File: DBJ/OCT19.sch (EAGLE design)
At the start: 30 parts, among them IC1 ATMEGA168TQFP-08, IC2 TB6612FNG, IC3 7805DT, J1 5.5x2.1mm Barrel, Y2 16MHZ

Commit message: Hbridge
entire hbridge circuit, changed any remaining thru-hole to smd, used a
different hbridge, organized the schematic,
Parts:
- removed IC2: TB6612FNG, adafruit:TB6612FNG
- removed LED1, LED2, LED3, PWR_LED, SCK_LED: (no value), eagle-ltspice:LED_E
- removed R7, R8: (no value), SparkFun-Resistors:RESISTORPTH-1/4W
- added C5: (no value), adafruit:C-US025-024X044
- added IC4: L298, st-microelectronics:L298
- added LD1, LD2: PL006-WCR12, led:PL006-WCR12
- added OK1, OK2: PC827, optocoupler:PC827
- added R2(SMD), R5, R6: (no value), adafruit:R-US_M0805
- added X1-MOT1, X2-MOT2: (no value), con-wago-500:W237-102
- C3: value 0.1uF -> (none); device SparkFun-Capacitors:0.1UF-25V(+80/-20%)(0603) -> adafruit:C-US025-024X044
- R1, R2, R3, R4: device SparkFun-Resistors:RESISTORPTH-1/4W -> adafruit:R-US_M0805
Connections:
- removed net N$12: PWR_LED.C, R8.1
- new net N$13: IC4.SEN_A, R5.1
- new net N$14: IC4.SEN_B, R6.1
- new net N$15: IC4.OUT2, X2-MOT2-1.KL
- new net N$2: LD2.A, R2.2
- new net N$3: OK1A.A, R3.1
- new net N$4: IC4.ENABLE_A, OK1A.COL
- new net N$5: OK2A.A, R4.1
- new net N$6: IC4.ENABLE_B, OK2A.COL
- new net N$7: IC4.OUT1, X2-MOT2-2.KL
- new net N$8: IC4.OUT3, X1-MOT1-2.KL
- new net N$9: IC4.OUT4, X1-MOT1-1.KL
- net +12V: now also C5.1, IC4.VS
- net +5V: now also C3.1, IC4.INPUT1, IC4.INPUT2, IC4.INPUT3, IC4.INPUT4, IC4.VCC, R2(SMD).2, R2.1; no longer PWR_LED.A, R1.2
- net GND: now also C3.2, C4.1, C5.2, IC4.GND, LD1.C, LD2.C, OK1A.C, OK1A.EMIT, OK2A.C, OK2A.EMIT, R5.2, R6.2; no longer R8.2, SCK_LED.C
- net N$1: now also R2(SMD).1; no longer R1.1
- net N$10: now also LD1.A, R1.1; no longer R7.2, SCK_LED.A
- net PD4: now also R4.2
- net PD5: now also R3.2
- net SCK: now also R1.2; no longer R7.1
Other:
- note added: "Barrel-Jack and Voltage Regulation"
- note added: "HBridge/Motor Controls"
- note added: "LCD"
- note added: "LED Indicators"
- moved on the sheet: C1, C2, C3, C4, IC1, IC3, ISP1, J1, R1, R2, R3, R4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

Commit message: Add files via upload
Redid the crystal wiring, and edited the RST of the ICSP
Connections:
- removed net XTAL1: IC1.PB6(XTAL1/TOSC1), Y2.3
- removed net XTAL2: IC1.PB7(XTAL2/TOSC2), Y2.1
- new net N$11: IC1.PB6(XTAL1/TOSC1), Y2.1
- new net N$16: IC1.PB7(XTAL2/TOSC2), Y2.3
- new net N$17: C4.1, ISP1.RST
- net GND: no longer C4.1
- net N$1: no longer ISP1.RST
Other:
- moved on the sheet: Y2
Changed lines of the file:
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@@
 <?xml version="1.0" encoding="utf-8"?>
 <!DOCTYPE eagle SYSTEM "eagle.dtd">
-<eagle version="7.7.0">
+<eagle version="7.6.0">
 <drawing>
 <settings>
@@
 <part name="CN4" library="adafruit" deviceset="JST_3PIN" device=""/>
 <part name="OK1" library="optocoupler" deviceset="PC827" device=""/>
-<part name="GND14" library="supply1" deviceset="GND" device=""/>
 <part name="R2(SMD)" library="adafruit" deviceset="R-US_" device="M0805"/>
 <part name="R1" library="adafruit" deviceset="R-US_" device="M0805"/>
@@
 <instance part="P+2" gate="1" x="96.52" y="195.58"/>
 <instance part="GND1" gate="1" x="83.82" y="177.8"/>
-<instance part="Y2" gate="G$1" x="162.56" y="129.54" rot="R270"/>
-<instance part="GND2" gate="1" x="152.4" y="124.46"/>
+<instance part="Y2" gate="G$1" x="182.88" y="129.54" rot="R270"/>
+<instance part="GND2" gate="1" x="167.64" y="124.46"/>
 <instance part="GND3" gate="1" x="187.96" y="96.52"/>
 <instance part="C1" gate="G$1" x="101.6" y="185.42"/>
@@
 <instance part="CN4" gate="G$1" x="345.44" y="101.6" rot="MR0"/>
 <instance part="OK1" gate="A" x="76.2" y="259.08" rot="R270"/>
-<instance part="GND14" gate="1" x="170.18" y="157.48" rot="R270"/>
 <instance part="R2(SMD)" gate="G$1" x="187.96" y="165.1" rot="R90"/>
 <instance part="R1" gate="G$1" x="320.04" y="187.96" rot="R90"/>
@@
 </segment>
 </net>
-<net name="XTAL1" class="0">
-<segment>
-<pinref part="IC1" gate="G$1" pin="PB6(XTAL1/TOSC1)"/>
-<wire x1="190.5" y1="132.08" x2="182.88" y2="132.08" width="0.1524" layer="91"/>
-<label x="182.88" y="132.08" size="1.778" layer="95"/>
-</segment>
-<segment>
-<pinref part="Y2" gate="G$1" pin="3"/>
-<wire x1="162.56" y1="127" x2="167.64" y2="127" width="0.1524" layer="91"/>
-<label x="167.64" y="127" size="1.778" layer="95"/>
-</segment>
-</net>
-<net name="XTAL2" class="0">
-<segment>
-<pinref part="IC1" gate="G$1" pin="PB7(XTAL2/TOSC2)"/>
-<wire x1="190.5" y1="127" x2="185.42" y2="127" width="0.1524" layer="91"/>
-<label x="185.42" y="127" size="1.778" layer="95"/>
-</segment>
-<segment>
-<pinref part="Y2" gate="G$1" pin="1"/>
-<wire x1="162.56" y1="132.08" x2="167.64" y2="132.08" width="0.1524" layer="91"/>
-<label x="165.1" y="132.08" size="1.778" layer="95"/>
-</segment>
-</net>
 <net name="GND" class="0">
-<segment>
-<pinref part="Y2" gate="G$1" pin="2"/>
-<pinref part="GND2" gate="1" pin="GND"/>
-<wire x1="154.94" y1="129.54" x2="152.4" y2="129.54" width="0.1524" layer="91"/>
-<wire x1="152.4" y1="129.54" x2="152.4" y2="127" width="0.1524" layer="91"/>
-</segment>
 <segment>
 <pinref part="GND3" gate="1" pin="GND"/>
@@
 </segment>
 <segment>
-<pinref part="C4" gate="G$1" pin="1"/>
-<pinref part="GND14" gate="1" pin="GND"/>
-<wire x1="172.72" y1="157.48" x2="175.26" y2="157.48" width="0.1524" layer="91"/>
-</segment>
-<segment>
 <pinref part="C3" gate="G$1" pin="2"/>
 <pinref part="GND16" gate="1" pin="GND"/>
@@
 <pinref part="GND23" gate="1" pin="GND"/>
 <wire x1="134.62" y1="210.82" x2="134.62" y2="213.36" width="0.2032" layer="91"/>
+</segment>
+<segment>
+<pinref part="Y2" gate="G$1" pin="2"/>
+<pinref part="GND2" gate="1" pin="GND"/>
+<wire x1="175.26" y1="129.54" x2="167.64" y2="129.54" width="0.1524" layer="91"/>
+<wire x1="167.64" y1="129.54" x2="167.64" y2="127" width="0.1524" layer="91"/>
 </segment>
 </net>
@@
 <junction x="187.96" y="157.48"/>
 <pinref part="C4" gate="G$1" pin="2"/>
-<pinref part="ISP1" gate="G$1" pin="RST"/>
-<wire x1="205.74" y1="175.26" x2="190.5" y2="175.26" width="0.1524" layer="91"/>
-<wire x1="190.5" y1="175.26" x2="190.5" y2="157.48" width="0.1524" layer="91"/>
-<junction x="190.5" y="157.48"/>
 <pinref part="R2(SMD)" gate="G$1" pin="1"/>
 </segment>
@@
 </segment>
 </net>
+<net name="N$11" class="0">
+<segment>
+<pinref part="Y2" gate="G$1" pin="1"/>
+<pinref part="IC1" gate="G$1" pin="PB6(XTAL1/TOSC1)"/>
+<wire x1="182.88" y1="132.08" x2="190.5" y2="132.08" width="0.1524" layer="91"/>
+</segment>
+</net>
+<net name="N$16" class="0">
+<segment>
+<pinref part="Y2" gate="G$1" pin="3"/>
+<pinref part="IC1" gate="G$1" pin="PB7(XTAL2/TOSC2)"/>
+<wire x1="182.88" y1="127" x2="190.5" y2="127" width="0.1524" layer="91"/>
+</segment>
+</net>
+<net name="N$17" class="0">
+<segment>
+<pinref part="C4" gate="G$1" pin="1"/>
+<wire x1="172.72" y1="157.48" x2="175.26" y2="157.48" width="0.1524" layer="91"/>
+<pinref part="ISP1" gate="G$1" pin="RST"/>
+<wire x1="205.74" y1="175.26" x2="190.5" y2="175.26" width="0.1524" layer="91"/>
+<wire x1="190.5" y1="175.26" x2="190.5" y2="185.42" width="0.1524" layer="91"/>
+<wire x1="190.5" y1="185.42" x2="172.72" y2="185.42" width="0.1524" layer="91"/>
+<wire x1="172.72" y1="185.42" x2="172.72" y2="157.48" width="0.1524" layer="91"/>
+</segment>
+</net>

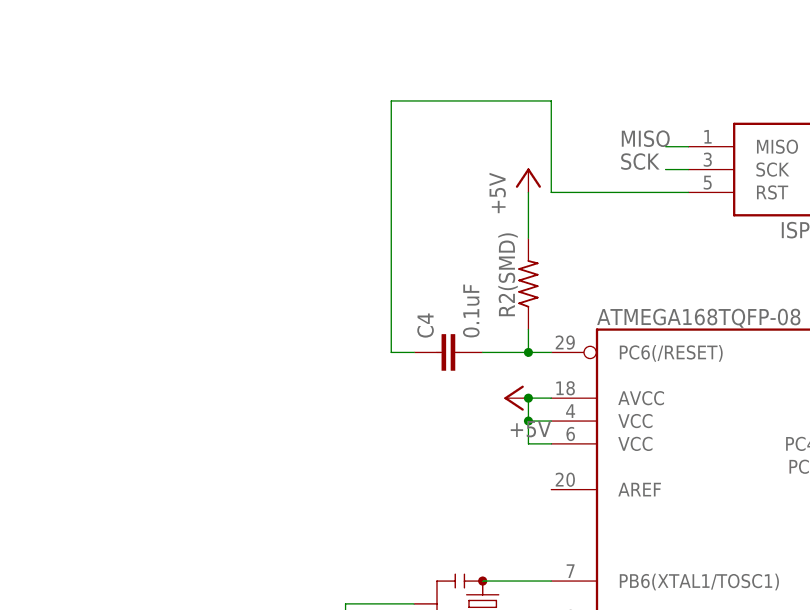
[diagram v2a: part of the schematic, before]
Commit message: sunday changes
added a push button to pc6/reset for human-interaction with the reset
line
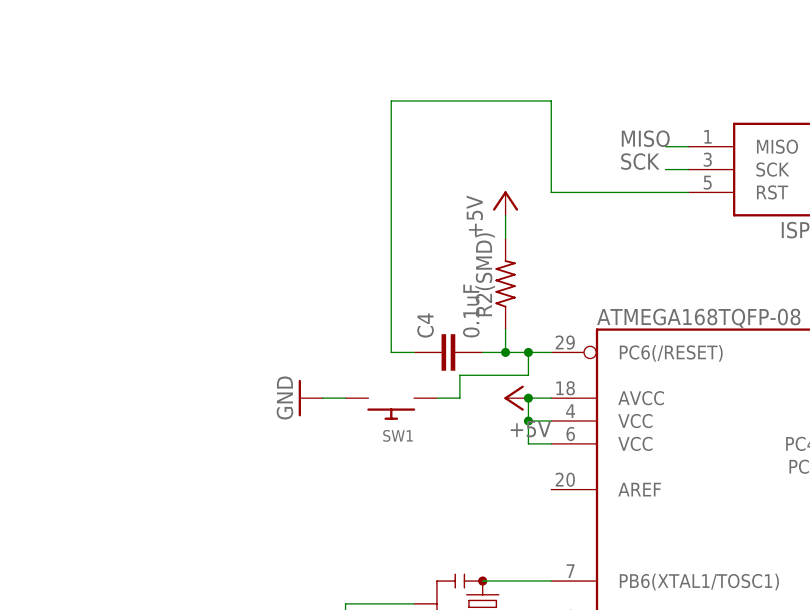
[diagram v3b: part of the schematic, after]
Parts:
- added SW1: (no value), adafruit:SWITCH_PUSHBUTTONC&K_KSS
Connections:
- net GND: now also SW1.P$2
- net N$1: now also SW1.P$1
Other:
- moved on the sheet: R2(SMD)
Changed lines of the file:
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@@
 <?xml version="1.0" encoding="utf-8"?>
 <!DOCTYPE eagle SYSTEM "eagle.dtd">
-<eagle version="7.6.0">
+<eagle version="7.7.0">
 <drawing>
 <settings>
@@
 <part name="P+13" library="supply1" deviceset="+12V" device=""/>
 <part name="P+14" library="supply1" deviceset="+5V" device=""/>
+<part name="SW1" library="adafruit" deviceset="SWITCH_PUSHBUTTON" device="C&amp;K_KSS"/>
+<part name="GND14" library="supply1" deviceset="GND" device=""/>
 </parts>
 <sheets>
@@
 <instance part="C4" gate="G$1" x="180.34" y="157.48" rot="R90"/>
 <instance part="P+3" gate="1" x="185.42" y="152.4" rot="R90"/>
-<instance part="P+4" gate="1" x="187.96" y="177.8"/>
+<instance part="P+4" gate="1" x="185.42" y="175.26"/>
 <instance part="GND8" gate="1" x="238.76" y="170.18"/>
 <instance part="P+6" gate="1" x="233.68" y="187.96"/>
@@
 <instance part="CN4" gate="G$1" x="345.44" y="101.6" rot="MR0"/>
 <instance part="OK1" gate="A" x="76.2" y="259.08" rot="R270"/>
-<instance part="R2(SMD)" gate="G$1" x="187.96" y="165.1" rot="R90"/>
+<instance part="R2(SMD)" gate="G$1" x="185.42" y="165.1" rot="R90"/>
 <instance part="R1" gate="G$1" x="320.04" y="187.96" rot="R90"/>
 <instance part="R2" gate="G$1" x="330.2" y="187.96" rot="R270"/>
@@
 <instance part="P+13" gate="1" x="134.62" y="238.76"/>
 <instance part="P+14" gate="1" x="76.2" y="238.76" rot="R90"/>
+<instance part="SW1" gate="G$1" x="172.72" y="152.4" rot="R180"/>
+<instance part="GND14" gate="1" x="162.56" y="152.4" rot="R270"/>
 </instances>
 <busses>
@@
 <wire x1="167.64" y1="129.54" x2="167.64" y2="127" width="0.1524" layer="91"/>
 </segment>
+<segment>
+<pinref part="GND14" gate="1" pin="GND"/>
+<pinref part="SW1" gate="G$1" pin="P$2"/>
+<wire x1="165.1" y1="152.4" x2="167.64" y2="152.4" width="0.2032" layer="91"/>
+</segment>
 </net>
 <net name="+5V" class="0">
@@
 <segment>
 <pinref part="P+4" gate="1" pin="+5V"/>
-<wire x1="187.96" y1="175.26" x2="187.96" y2="170.18" width="0.1524" layer="91"/>
+<wire x1="185.42" y1="172.72" x2="185.42" y2="170.18" width="0.1524" layer="91"/>
 <pinref part="R2(SMD)" gate="G$1" pin="2"/>
 </segment>
@@
 <segment>
 <pinref part="IC1" gate="G$1" pin="PC6(/RESET)"/>
-<wire x1="182.88" y1="157.48" x2="187.96" y2="157.48" width="0.1524" layer="91"/>
+<wire x1="182.88" y1="157.48" x2="185.42" y2="157.48" width="0.1524" layer="91"/>
+<wire x1="185.42" y1="157.48" x2="187.96" y2="157.48" width="0.1524" layer="91"/>
 <wire x1="187.96" y1="157.48" x2="190.5" y2="157.48" width="0.1524" layer="91"/>
-<wire x1="187.96" y1="160.02" x2="187.96" y2="157.48" width="0.1524" layer="91"/>
-<junction x="187.96" y="157.48"/>
+<wire x1="185.42" y1="160.02" x2="185.42" y2="157.48" width="0.1524" layer="91"/>
+<junction x="185.42" y="157.48"/>
 <pinref part="C4" gate="G$1" pin="2"/>
 <pinref part="R2(SMD)" gate="G$1" pin="1"/>
+<junction x="187.96" y="157.48"/>
+<wire x1="187.96" y1="157.48" x2="187.96" y2="154.94" width="0.2032" layer="91"/>
+<wire x1="187.96" y1="154.94" x2="180.34" y2="154.94" width="0.2032" layer="91"/>
+<wire x1="180.34" y1="154.94" x2="180.34" y2="152.4" width="0.2032" layer="91"/>
+<pinref part="SW1" gate="G$1" pin="P$1"/>
+<wire x1="180.34" y1="152.4" x2="177.8" y2="152.4" width="0.2032" layer="91"/>
 </segment>
 </net>
